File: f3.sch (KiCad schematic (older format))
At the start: 13 parts, among them U6 STM32F303K8Tx, Y1 Crystal

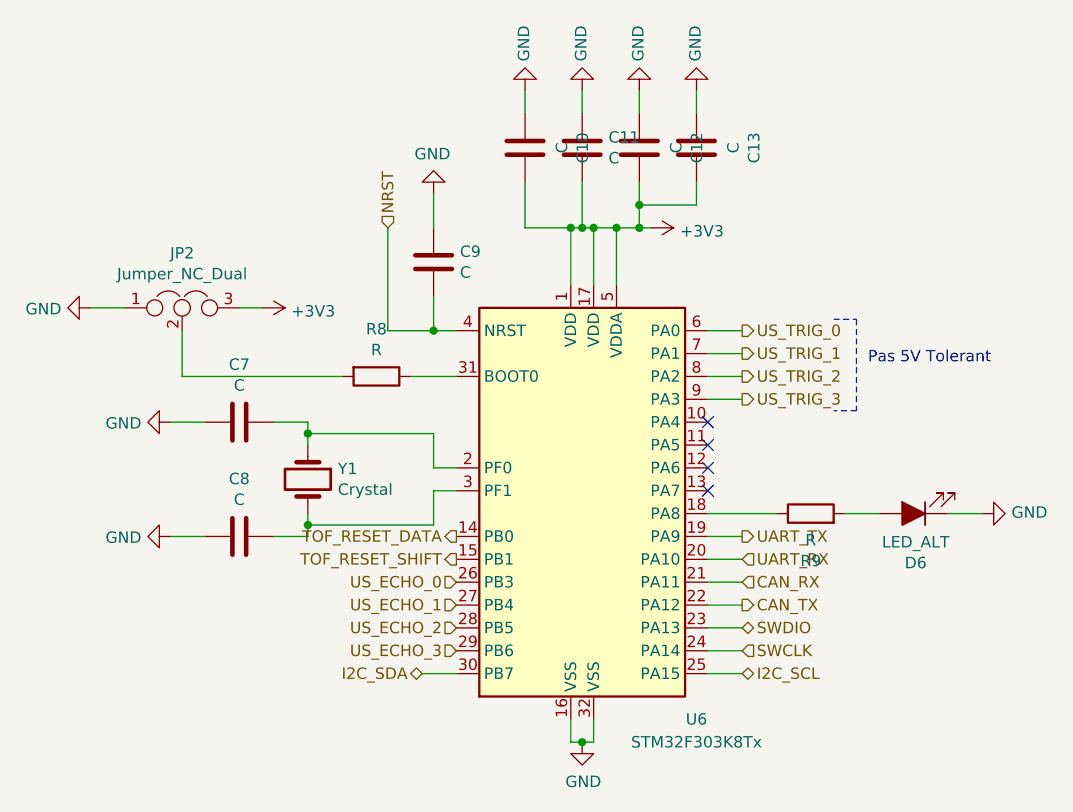
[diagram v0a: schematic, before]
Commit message: Added IC for level translation with ultrasonic sensors
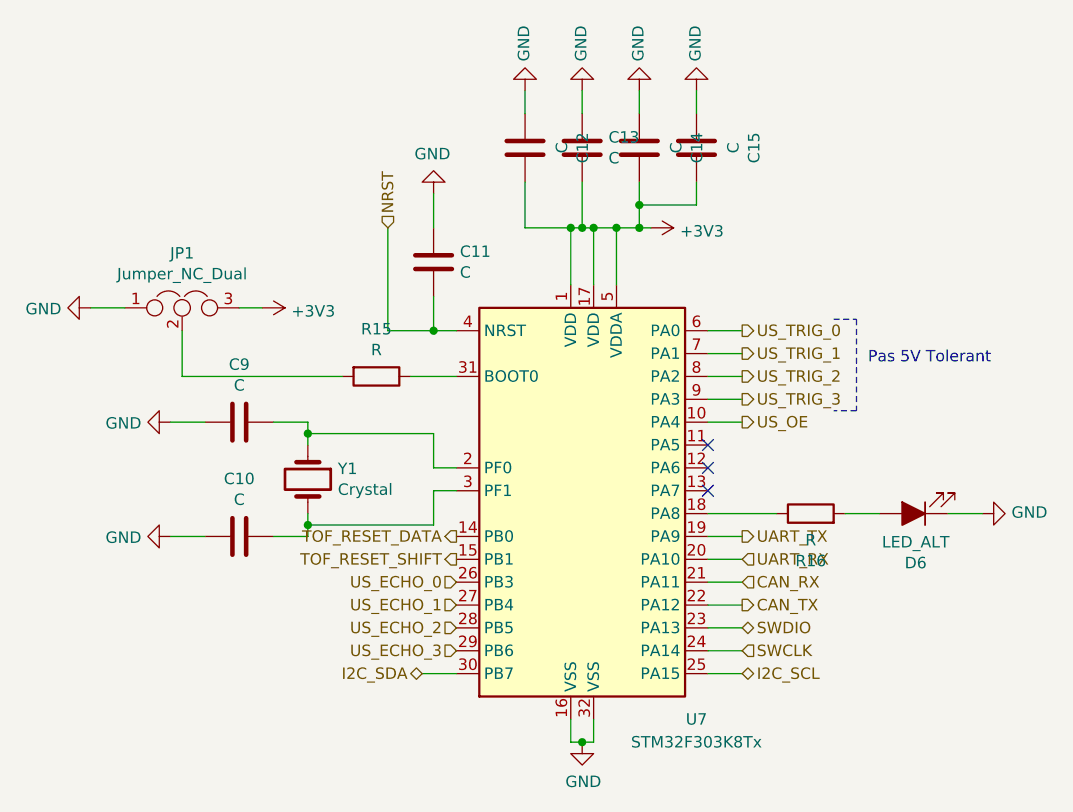
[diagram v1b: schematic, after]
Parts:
- C10: renamed from C8; footprint (none) -> Capacitor_SMD:C_0805_2012Metric_Pad1.15x1.40mm_HandSolder
- C11: renamed from C9; footprint (none) -> Capacitor_SMD:C_0805_2012Metric_Pad1.15x1.40mm_HandSolder
- C12: renamed from C10; footprint (none) -> Capacitor_SMD:C_0805_2012Metric_Pad1.15x1.40mm_HandSolder
- C13: renamed from C11; footprint (none) -> Capacitor_SMD:C_0805_2012Metric_Pad1.15x1.40mm_HandSolder
- C14: renamed from C12; footprint (none) -> Capacitor_SMD:C_0805_2012Metric_Pad1.15x1.40mm_HandSolder
- C15: renamed from C13; footprint (none) -> Capacitor_SMD:C_0805_2012Metric_Pad1.15x1.40mm_HandSolder
- C9: renamed from C7; footprint (none) -> Capacitor_SMD:C_0805_2012Metric_Pad1.15x1.40mm_HandSolder
- D6: footprint (none) -> LED_SMD:LED_0805_2012Metric_Castellated
- JP1: renamed from JP2; footprint (none) -> Connector_PinHeader_2.54mm:PinHeader_1x03_P2.54mm_Vertical
- R15: renamed from R8; footprint (none) -> Resistor_SMD:R_0805_2012Metric_Pad1.15x1.40mm_HandSolder
- R16: renamed from R9; footprint (none) -> Resistor_SMD:R_0805_2012Metric_Pad1.15x1.40mm_HandSolder
- renumbered U6 to U7
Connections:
- net US_OE: now reaches U7.10 (PA4)
- no-connect marks 4 -> 3
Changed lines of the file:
@@
 $Descr A4 11693 8268
 encoding utf-8
-Sheet 19 19
+Sheet 17 19
 Title ""
 Date ""
@@
 $EndDescr
 $Comp
-L MCU_ST_STM32F3:STM32F303K8Tx U6
+L MCU_ST_STM32F3:STM32F303K8Tx U7
 U 1 1 5BBD3F5D
 P 5350 3800
-F 0 "U6" H 5800 2800 50  0000 C CNN
+F 0 "U7" H 5800 2800 50  0000 C CNN
 F 1 "STM32F303K8Tx" H 5800 2700 50  0000 C CNN
 F 2 "Package_QFP:LQFP-32_7x7mm_P0.8mm" H 4850 2900 50  0001 R CNN
@@
 $EndComp
 $Comp
-L Device:C C7
+L Device:C C9
 U 1 1 5BBD416E
 P 3800 3500
-F 0 "C7" V 3548 3500 50  0000 C CNN
+F 0 "C9" V 3548 3500 50  0000 C CNN
 F 1 "C" V 3639 3500 50  0000 C CNN
-F 2 "" H 3838 3350 50  0001 C CNN
+F 2 "Capacitor_SMD:C_0805_2012Metric_Pad1.15x1.40mm_HandSolder" H 3838 3350 50  0001 C CNN
 F 3 "~" H 3800 3500 50  0001 C CNN
 	1    3800 3500
@@
 $EndComp
 $Comp
-L Device:C C8
+L Device:C C10
 U 1 1 5BBD4205
 P 3800 4000
-F 0 "C8" V 3548 4000 50  0000 C CNN
+F 0 "C10" V 3548 4000 50  0000 C CNN
 F 1 "C" V 3639 4000 50  0000 C CNN
-F 2 "" H 3838 3850 50  0001 C CNN
+F 2 "Capacitor_SMD:C_0805_2012Metric_Pad1.15x1.40mm_HandSolder" H 3838 3850 50  0001 C CNN
 F 3 "~" H 3800 4000 50  0001 C CNN
 	1    3800 4000
@@
 $EndComp
 $Comp
-L power:GND #PWR029
+L power:GND #PWR059
 U 1 1 5BBD4293
 P 3500 3500
-F 0 "#PWR029" H 3500 3250 50  0001 C CNN
+F 0 "#PWR059" H 3500 3250 50  0001 C CNN
 F 1 "GND" V 3505 3372 50  0000 R CNN
 F 2 "" H 3500 3500 50  0001 C CNN
@@
 $EndComp
 $Comp
-L power:GND #PWR030
+L power:GND #PWR060
 U 1 1 5BBD42C5
 P 3500 4000
-F 0 "#PWR030" H 3500 3750 50  0001 C CNN
+F 0 "#PWR060" H 3500 3750 50  0001 C CNN
 F 1 "GND" V 3505 3872 50  0000 R CNN
 F 2 "" H 3500 4000 50  0001 C CNN
@@
 	4100 3950 4100 3900
 $Comp
-L Device:R R8
+L Device:R R15
 U 1 1 5BBD441A
 P 4400 3300
-F 0 "R8" V 4193 3300 50  0000 C CNN
+F 0 "R15" V 4193 3300 50  0000 C CNN
 F 1 "R" V 4284 3300 50  0000 C CNN
-F 2 "" V 4330 3300 50  0001 C CNN
+F 2 "Resistor_SMD:R_0805_2012Metric_Pad1.15x1.40mm_HandSolder" V 4330 3300 50  0001 C CNN
 F 3 "~" H 4400 3300 50  0001 C CNN
 	1    4400 3300
@@
 $EndComp
 $Comp
-L Device:Jumper_NC_Dual JP2
+L Device:Jumper_NC_Dual JP1
 U 1 1 5BBD452E
 P 3550 3000
-F 0 "JP2" H 3550 3239 50  0000 C CNN
+F 0 "JP1" H 3550 3239 50  0000 C CNN
 F 1 "Jumper_NC_Dual" H 3550 3148 50  0000 C CNN
-F 2 "" H 3550 3000 50  0001 C CNN
+F 2 "Connector_PinHeader_2.54mm:PinHeader_1x03_P2.54mm_Vertical" H 3550 3000 50  0001 C CNN
 F 3 "~" H 3550 3000 50  0001 C CNN
 	1    3550 3000
@@
 	4550 3300 4750 3300
 $Comp
-L power:GND #PWR028
+L power:GND #PWR058
 U 1 1 5BBD4A9A
 P 3150 3000
-F 0 "#PWR028" H 3150 2750 50  0001 C CNN
+F 0 "#PWR058" H 3150 2750 50  0001 C CNN
 F 1 "GND" V 3155 2872 50  0000 R CNN
 F 2 "" H 3150 3000 50  0001 C CNN
@@
 	3150 3000 3300 3000
 $Comp
-L power:+3V3 #PWR031
+L power:+3V3 #PWR061
 U 1 1 5BBD4C69
 P 3900 3000
-F 0 "#PWR031" H 3900 2850 50  0001 C CNN
+F 0 "#PWR061" H 3900 2850 50  0001 C CNN
 F 1 "+3V3" V 3915 3128 50  0000 L CNN
 F 2 "" H 3900 3000 50  0001 C CNN
@@
 NRST
 $Comp
-L Device:C C9
+L Device:C C11
 U 1 1 5BBD5511
 P 4650 2800
-F 0 "C9" H 4765 2846 50  0000 L CNN
+F 0 "C11" H 4765 2846 50  0000 L CNN
 F 1 "C" H 4765 2755 50  0000 L CNN
-F 2 "" H 4688 2650 50  0001 C CNN
+F 2 "Capacitor_SMD:C_0805_2012Metric_Pad1.15x1.40mm_HandSolder" H 4688 2650 50  0001 C CNN
 F 3 "~" H 4650 2800 50  0001 C CNN
 	1    4650 2800
@@
 $EndComp
 $Comp
-L power:GND #PWR032
+L power:GND #PWR062
 U 1 1 5BBD55CA
 P 4650 2500
-F 0 "#PWR032" H 4650 2250 50  0001 C CNN
+F 0 "#PWR062" H 4650 2250 50  0001 C CNN
 F 1 "GND" H 4655 2327 50  0000 C CNN
 F 2 "" H 4650 2500 50  0001 C CNN
@@
 	5350 2650 5450 2650
 $Comp
-L power:+3V3 #PWR037
+L power:+3V3 #PWR067
 U 1 1 5BBD6204
 P 5600 2650
-F 0 "#PWR037" H 5600 2500 50  0001 C CNN
+F 0 "#PWR067" H 5600 2500 50  0001 C CNN
 F 1 "+3V3" V 5615 2778 50  0000 L CNN
 F 2 "" H 5600 2650 50  0001 C CNN
@@
 Connection ~ 5450 2650
 $Comp
-L Device:C C10
+L Device:C C12
 U 1 1 5BBD657B
 P 5050 2300
-F 0 "C10" V 4798 2300 50  0000 C CNN
+F 0 "C12" V 4798 2300 50  0000 C CNN
 F 1 "C" V 4889 2300 50  0000 C CNN
-F 2 "" H 5088 2150 50  0001 C CNN
+F 2 "Capacitor_SMD:C_0805_2012Metric_Pad1.15x1.40mm_HandSolder" H 5088 2150 50  0001 C CNN
 F 3 "~" H 5050 2300 50  0001 C CNN
 	1    5050 2300
@@
 $EndComp
 $Comp
-L Device:C C11
+L Device:C C13
 U 1 1 5BBD660C
 P 5300 2300
-F 0 "C11" H 5185 2346 50  0000 R CNN
+F 0 "C13" H 5185 2346 50  0000 R CNN
 F 1 "C" H 5185 2255 50  0000 R CNN
-F 2 "" H 5338 2150 50  0001 C CNN
+F 2 "Capacitor_SMD:C_0805_2012Metric_Pad1.15x1.40mm_HandSolder" H 5338 2150 50  0001 C CNN
 F 3 "~" H 5300 2300 50  0001 C CNN
 	1    5300 2300
@@
 $EndComp
 $Comp
-L Device:C C12
+L Device:C C14
 U 1 1 5BBD669F
 P 5550 2300
-F 0 "C12" V 5298 2300 50  0000 C CNN
+F 0 "C14" V 5298 2300 50  0000 C CNN
 F 1 "C" V 5389 2300 50  0000 C CNN
-F 2 "" H 5588 2150 50  0001 C CNN
+F 2 "Capacitor_SMD:C_0805_2012Metric_Pad1.15x1.40mm_HandSolder" H 5588 2150 50  0001 C CNN
 F 3 "~" H 5550 2300 50  0001 C CNN
 	1    5550 2300
@@
 $EndComp
 $Comp
-L Device:C C13
+L Device:C C15
 U 1 1 5BBD681C
 P 5800 2300
-F 0 "C13" V 5548 2300 50  0000 C CNN
+F 0 "C15" V 5548 2300 50  0000 C CNN
 F 1 "C" V 5639 2300 50  0000 C CNN
-F 2 "" H 5838 2150 50  0001 C CNN
+F 2 "Capacitor_SMD:C_0805_2012Metric_Pad1.15x1.40mm_HandSolder" H 5838 2150 50  0001 C CNN
 F 3 "~" H 5800 2300 50  0001 C CNN
 	1    5800 2300
@@
 $EndComp
 $Comp
-L power:GND #PWR038
+L power:GND #PWR068
 U 1 1 5BBD68AE
 P 5800 2050
-F 0 "#PWR038" H 5800 1800 50  0001 C CNN
+F 0 "#PWR068" H 5800 1800 50  0001 C CNN
 F 1 "GND" V 5805 1922 50  0000 R CNN
 F 2 "" H 5800 2050 50  0001 C CNN
@@
 $EndComp
 $Comp
-L power:GND #PWR036
+L power:GND #PWR066
 U 1 1 5BBD68FC
 P 5550 2050
-F 0 "#PWR036" H 5550 1800 50  0001 C CNN
+F 0 "#PWR066" H 5550 1800 50  0001 C CNN
 F 1 "GND" V 5555 1922 50  0000 R CNN
 F 2 "" H 5550 2050 50  0001 C CNN
@@
 $EndComp
 $Comp
-L power:GND #PWR034
+L power:GND #PWR064
 U 1 1 5BBD694A
 P 5300 2050
-F 0 "#PWR034" H 5300 1800 50  0001 C CNN
+F 0 "#PWR064" H 5300 1800 50  0001 C CNN
 F 1 "GND" V 5305 1922 50  0000 R CNN
 F 2 "" H 5300 2050 50  0001 C CNN
@@
 $EndComp
 $Comp
-L power:GND #PWR033
+L power:GND #PWR063
 U 1 1 5BBD6998
 P 5050 2050
-F 0 "#PWR033" H 5050 1800 50  0001 C CNN
+F 0 "#PWR063" H 5050 1800 50  0001 C CNN
 F 1 "GND" V 5055 1922 50  0000 R CNN
 F 2 "" H 5050 2050 50  0001 C CNN
@@
 	5550 2550 5550 2650
 $Comp
-L power:GND #PWR035
+L power:GND #PWR065
 U 1 1 5BBDA4B0
 P 5300 4900
-F 0 "#PWR035" H 5300 4650 50  0001 C CNN
+F 0 "#PWR065" H 5300 4650 50  0001 C CNN
 F 1 "GND" H 5305 4727 50  0000 C CNN
 F 2 "" H 5300 4900 50  0001 C CNN
@@
 Connection ~ 5300 4900
 $Comp
-L Device:R R9
+L Device:R R16
 U 1 1 5BBDC2CE
 P 6300 3900
-F 0 "R9" V 6093 3900 50  0000 C CNN
+F 0 "R16" V 6093 3900 50  0000 C CNN
 F 1 "R" V 6184 3900 50  0000 C CNN
-F 2 "" V 6230 3900 50  0001 C CNN
+F 2 "Resistor_SMD:R_0805_2012Metric_Pad1.15x1.40mm_HandSolder" V 6230 3900 50  0001 C CNN
 F 3 "~" H 6300 3900 50  0001 C CNN
 	1    6300 3900
@@
 $EndComp
 $Comp
-L power:GND #PWR039
+L power:GND #PWR069
 U 1 1 5BBDC410
 P 7050 3900
-F 0 "#PWR039" H 7050 3650 50  0001 C CNN
+F 0 "#PWR069" H 7050 3650 50  0001 C CNN
 F 1 "GND" V 7055 3772 50  0000 R CNN
 F 2 "" H 7050 3900 50  0001 C CNN
@@
 F 0 "D6" H 6741 4116 50  0000 C CNN
 F 1 "LED_ALT" H 6741 4025 50  0000 C CNN
-F 2 "" H 6750 3900 50  0001 C CNN
+F 2 "LED_SMD:LED_0805_2012Metric_Castellated" H 6750 3900 50  0001 C CNN
 F 3 "~" H 6750 3900 50  0001 C CNN
 	1    6750 3900
@@
 NoConn ~ 5850 3700
 NoConn ~ 5850 3600
-NoConn ~ 5850 3500
 Text Notes 6550 3250 0    50   ~ 0
 Pas 5V Tolerant
@@
 Wire Notes Line
 	6500 3450 6400 3450
+Text HLabel 6000 3500 2    50   Output ~ 0
+US_OE
+Wire Wire Line
+	5850 3500 6000 3500
 $EndSCHEMATC

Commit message: Footprint association
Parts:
- Y1: footprint (none) -> Crystal:Crystal_HC49-U_Vertical
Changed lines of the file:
@@
 I2C_SDA
-$Comp
-L Device:Crystal Y1
-U 1 1 5BBD409E
-P 4100 3750
-F 0 "Y1" V 4054 3881 50  0000 L CNN
-F 1 "Crystal" V 4145 3881 50  0000 L CNN
-F 2 "" H 4100 3750 50  0001 C CNN
-F 3 "~" H 4100 3750 50  0001 C CNN
-	1    4100 3750
-	0    1    1    0
-$EndComp
 $Comp
 L Device:C C9
@@
 	3500 4000 3650 4000
 Wire Wire Line
-	3950 4000 4100 4000
-Wire Wire Line
-	4100 4000 4100 3950
-Wire Wire Line
-	3950 3500 4100 3500
-Wire Wire Line
-	4100 3500 4100 3550
-Wire Wire Line
-	4100 3550 4650 3550
-Wire Wire Line
-	4650 3550 4650 3700
-Wire Wire Line
 	4650 3700 4750 3700
-Connection ~ 4100 3550
-Wire Wire Line
-	4100 3550 4100 3600
 Wire Wire Line
 	4750 3800 4650 3800
-Wire Wire Line
-	4650 3800 4650 3950
-Wire Wire Line
-	4650 3950 4100 3950
-Connection ~ 4100 3950
-Wire Wire Line
-	4100 3950 4100 3900
 $Comp
 L Device:R R15
@@
 Wire Wire Line
 	5850 3500 6000 3500
+Wire Wire Line
+	4650 3550 4650 3700
+Wire Wire Line
+	4650 3800 4650 3950
+Wire Wire Line
+	3950 4000 4100 4000
+Wire Wire Line
+	3950 3500 4100 3500
+Wire Wire Line
+	4100 3950 4100 3900
+Wire Wire Line
+	4100 4000 4100 3950
+Connection ~ 4100 3950
+Wire Wire Line
+	4650 3950 4100 3950
+Wire Wire Line
+	4100 3550 4100 3600
+Wire Wire Line
+	4100 3500 4100 3550
+Connection ~ 4100 3550
+Wire Wire Line
+	4100 3550 4650 3550
+$Comp
+L Device:Crystal Y1
+U 1 1 5BBD409E
+P 4100 3750
+F 0 "Y1" V 4054 3881 50  0000 L CNN
+F 1 "Crystal" V 4145 3881 50  0000 L CNN
+F 2 "Crystal:Crystal_HC49-U_Vertical" H 4100 3750 50  0001 C CNN
+F 3 "~" H 4100 3750 50  0001 C CNN
+	1    4100 3750
+	0    1    1    0
+$EndComp
 $EndSCHEMATC
